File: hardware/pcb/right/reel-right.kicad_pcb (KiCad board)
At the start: 2 copper layers, 145 x 88.1 mm, 47 parts, among them J1 Conn_01x02, J3 Conn_01x05, SW1 SW_Push, SW10 SW_Push, SW11 SW_Push, SW12 SW_Push, SW13 SW_Push, SW14 SW_Push, SW15 SW_Push, SW16 SW_Push, SW17 SW_Push, SW18 SW_Push, SW19 SW_Push, SW2 SW_Push, SW22 SW_SPDT, SW3 SW_Push, SW4 SW_Push, SW5 SW_Push, SW6 SW_Push, SW7 SW_Push, SW8 SW_Push, SW9 SW_Push

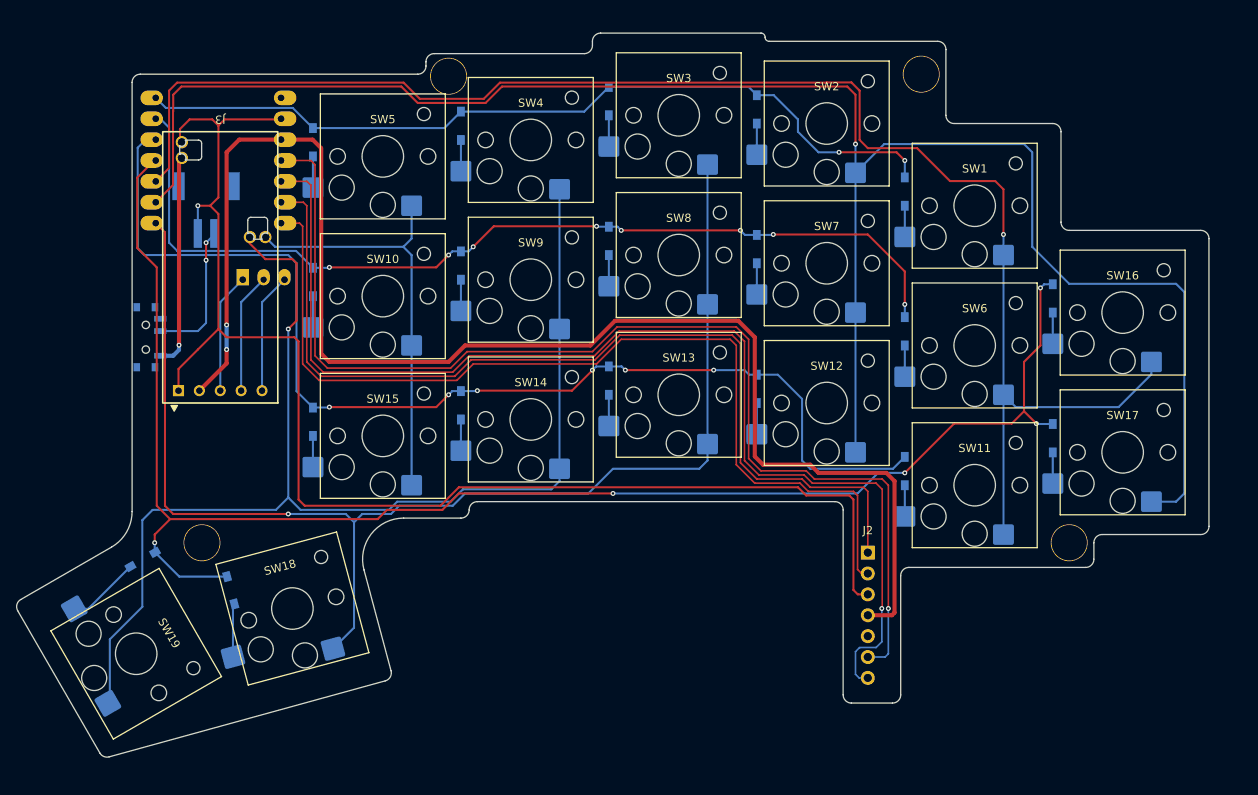
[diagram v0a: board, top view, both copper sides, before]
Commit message: Adjust right PCB edge and trackball routing
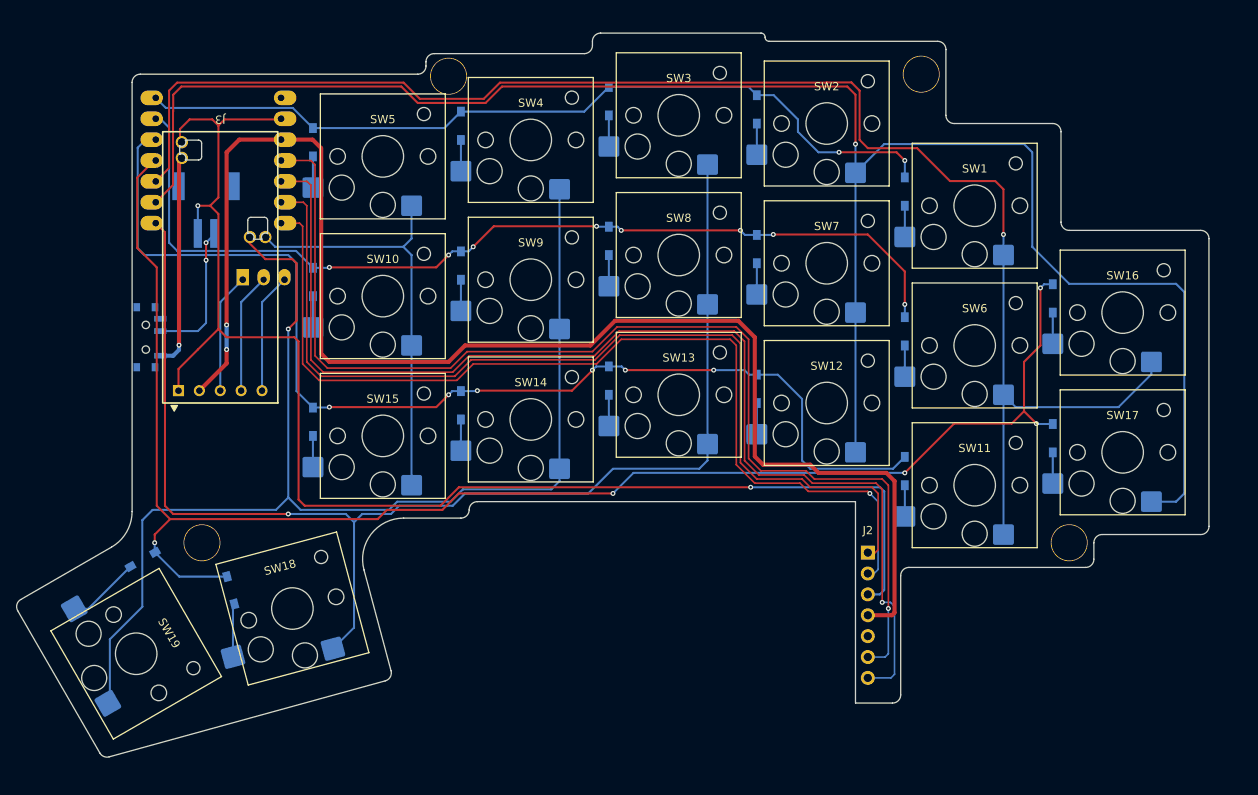
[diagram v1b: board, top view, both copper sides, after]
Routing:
- net GND: track 166.7 -> 171.3 mm, vias 1 -> 2
- net SCLK: track 117.2 -> 119.3 mm
- net nCS: track 116.8 -> 118.8 mm, vias 0 -> 1
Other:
- outline, holes or cut-outs redrawn

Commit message: Update PCB and side switch research
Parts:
- moved Ref** 19.6 mm to (165.0, 88.0)
- moved Ref** 17.2 mm to (88.0, 68.0)
- moved Ref** 13.5 mm to (145.0, 64.0)
- moved D1 6.87 mm to (146.5, 55.8)
- moved D19 5.83 mm to (50.2, 113.1)
- moved D18 4.43 mm to (59.5, 114.8)
- moved D16 4.12 mm to (165.5, 74.0)
- moved D17 4.12 mm to (165.5, 93.0)
- moved SW16 4.12 mm to (174.0, 78.5)
- moved SW17 4.12 mm to (174.0, 97.5)
- moved D11 3.61 mm to (146.5, 98.0)
- moved SW1 3.61 mm to (155.0, 64.5)
- moved SW11 3.61 mm to (155.0, 102.5)
- moved D6 3.00 mm to (146.5, 79.0)
- moved SW6 3.00 mm to (155.0, 83.5)
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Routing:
- net Row3: track 192.2 -> 0.00 mm, vias 5 -> 0
- net Col1: track 227.5 -> 38.0 mm, vias 1 -> 0
- net Col0: track 187.9 -> 64.2 mm, vias 1 -> 0
- net Col3: track 149.2 -> 38.0 mm, vias 1 -> 0
- net Row2: track 137.5 -> 100.8 mm, vias 6 -> 2
- net Row1: track 116.8 -> 138.3 mm, vias 8 -> 5
- net GND: track 171.3 -> 188.2 mm, vias 2 -> 3
- net Col2: track 157.2 -> 168.2 mm
- net 3.3V: track 176.1 -> 181.4 mm, vias 2 -> 0
- net Row0: track 101.4 -> 106.6 mm, vias 2 -> 0
- net Net-(D1-A): track 3.80 -> 9.01 mm
- net Net-(D19-A): track 8.98 -> 4.73 mm
- net nCS: track 118.8 -> 123.0 mm
- net Col4: track 51.8 -> 55.5 mm
- net SDIO: track 139.7 -> 142.9 mm
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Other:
- board size 145 x 88.1 mm -> 147.1 x 92.1 mm

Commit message: Update ReeL PCB and mechanical assets
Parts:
- moved J3 14.5 mm to (60.2, 103.5)
- moved Ref** 2.83 mm to (56.0, 109.5)
- moved SW19 0.71 mm to (49.5, 123.5)
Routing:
- net Row3: track 0.00 -> 206.5 mm, vias 0 -> 6
- net Col1: track 38.0 -> 205.8 mm, vias 0 -> 3
- net Col0: track 64.2 -> 204.0 mm, vias 0 -> 2
- net Col3: track 38.0 -> 150.0 mm, vias 0 -> 4
- net Row2: track 100.8 -> 145.7 mm, vias 2 -> 8
- net GND: track 188.2 -> 203.1 mm, vias 3 -> 5
- net SI: track 16.2 -> 30.7 mm
- net SCK: track 16.2 -> 30.7 mm
- net CS: track 16.2 -> 30.7 mm
- net 3.3V: track 181.4 -> 195.9 mm
- net Row0: track 106.6 -> 101.5 mm
- net Net-(D19-A): track 4.73 -> 5.44 mm
- net nCS: track 123.0 -> 122.4 mm
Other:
- board size 147.1 x 92.1 mm -> 147.7 x 92.6 mm

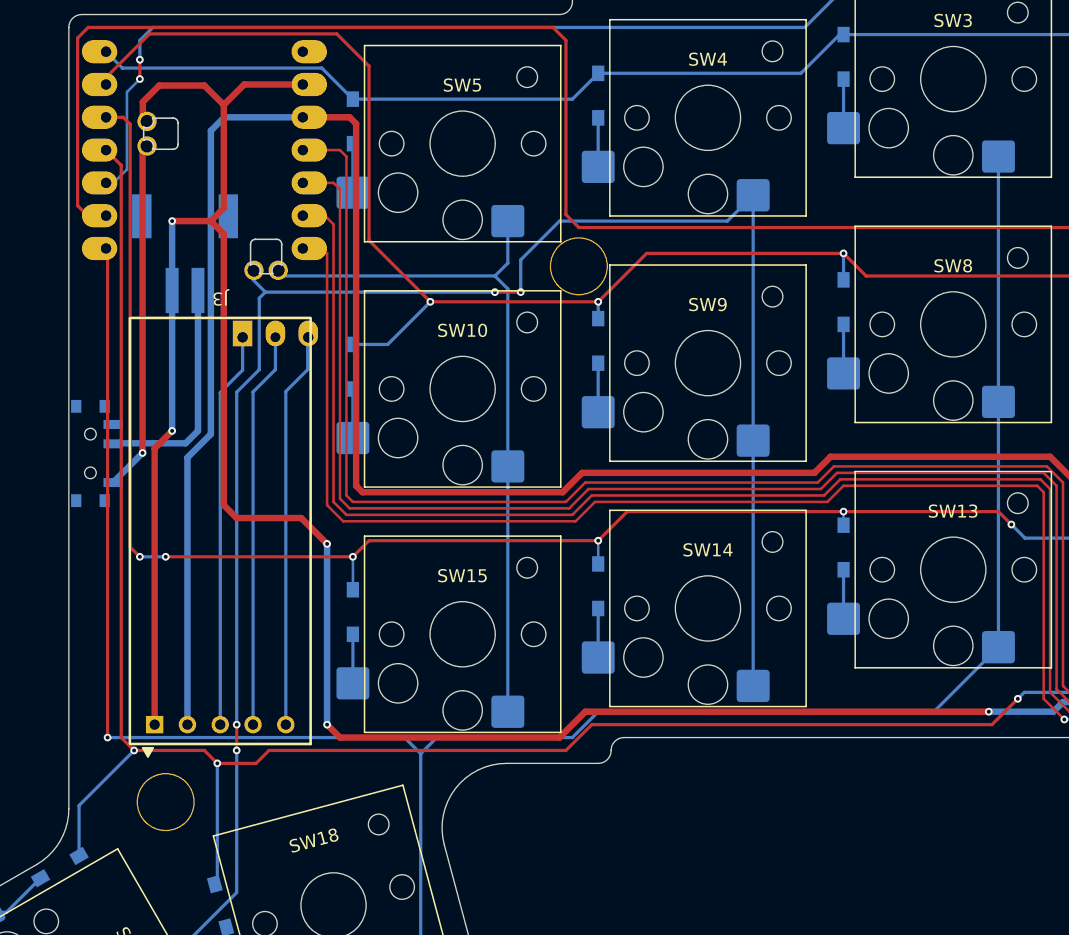
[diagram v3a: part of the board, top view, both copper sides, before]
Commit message: Correct ReeL PCB connector pinouts and routing
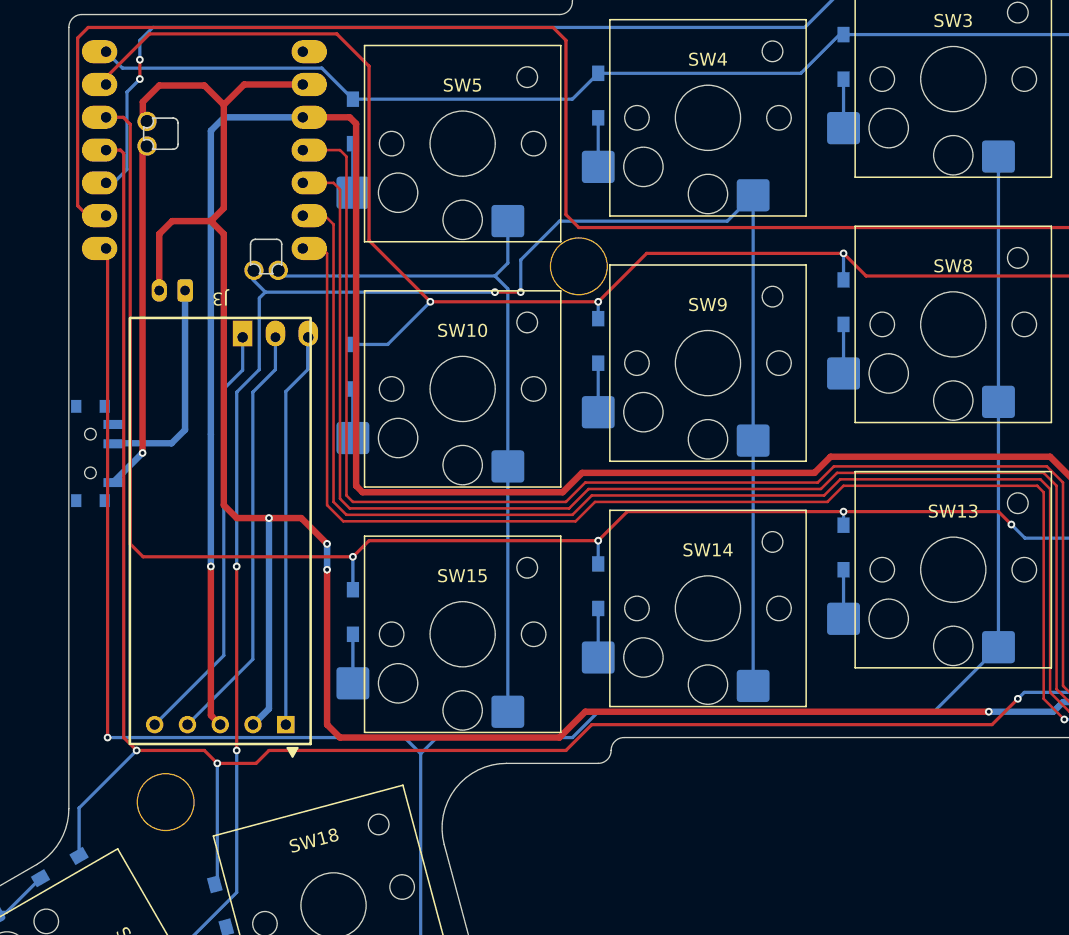
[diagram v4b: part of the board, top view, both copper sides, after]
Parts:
- J1: footprint reel:JST_S2B-PH-SM4-TB -> Connector_JST:JST_PH_S2B-PH-K_1x02_P2.00mm_Horizontal
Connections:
- J3 pad 1: GND -> SI
- J3 pad 2: 3.3V -> SCK
- J3 pad 3: SI -> 3.3V
- J3 pad 4: SCK -> GND
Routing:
- net GND: track 203.1 -> 185.9 mm, vias 5 -> 4
- net SI: track 30.7 -> 32.8 mm
- net SCK: track 30.7 -> 32.8 mm
- net Net-(J1-Pin_1): track 17.9 -> 16.8 mm
- net Row3: track 206.5 -> 207.2 mm
- net 3.3V: track 195.9 -> 195.4 mm, vias 0 -> 1
- net Row2: track 145.7 -> 145.5 mm, vias 8 -> 6
